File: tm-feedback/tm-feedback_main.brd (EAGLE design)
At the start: 60.1 x 40.3 mm, 45 parts

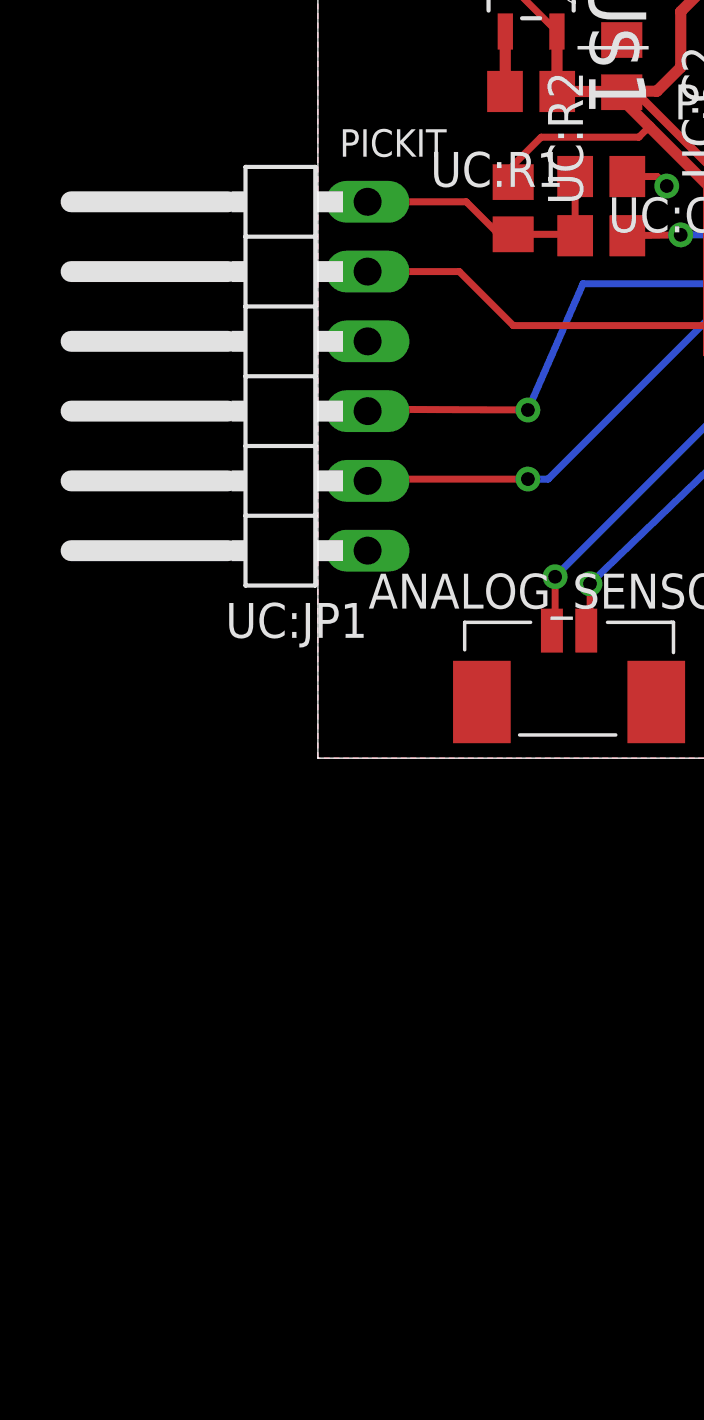
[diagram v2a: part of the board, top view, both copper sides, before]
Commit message: Replace PICKIT header with new header
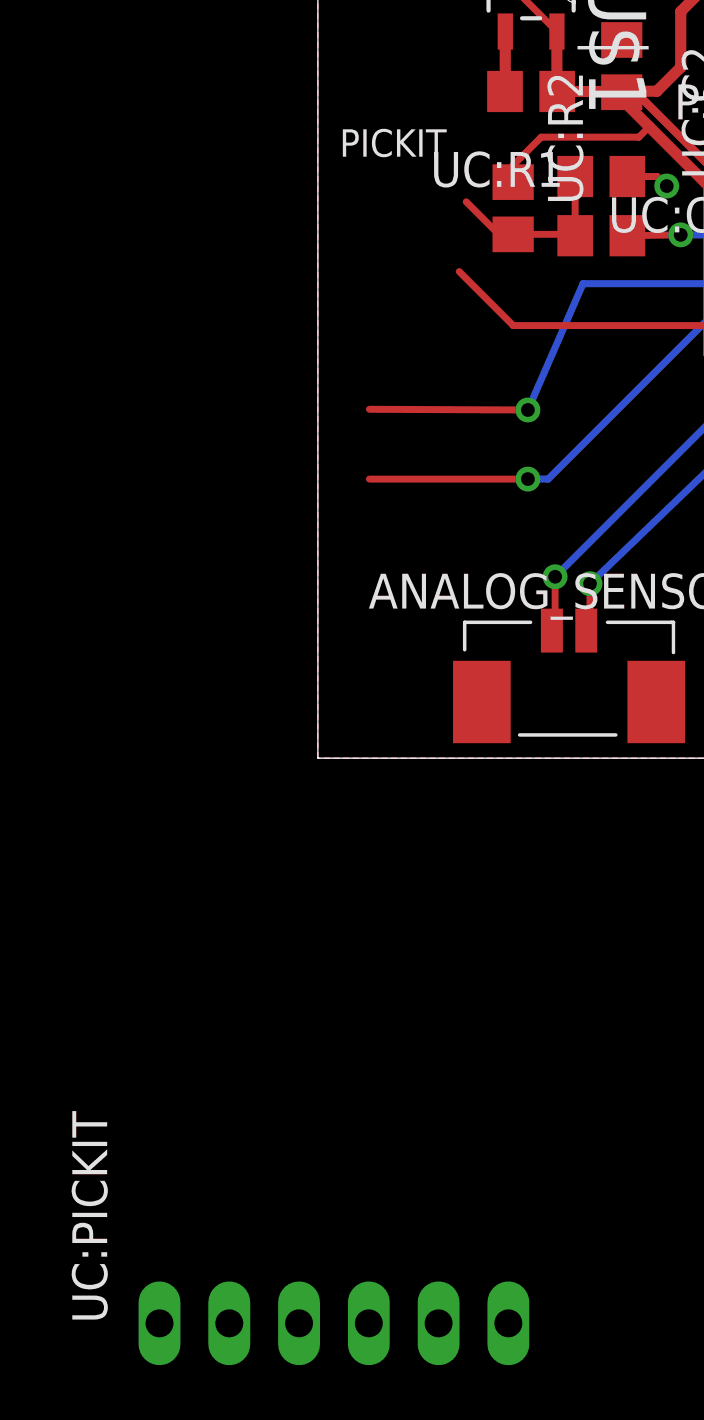
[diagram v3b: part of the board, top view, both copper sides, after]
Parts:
- removed UC:JP1: PICKIT, pinhead:1X06/90
- added UC:PICKIT: JP1, tactile-music:1X06/90
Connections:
- net +3V3: now also UC:PICKIT.5; no longer UC:JP1.5
- net GND: now also UC:PICKIT.4; no longer UC:JP1.4
- net UC:!MCLR: now also UC:PICKIT.6; no longer UC:JP1.6
- net UC:PGC: now also UC:PICKIT.2; no longer UC:JP1.2
- net UC:PGD: now also UC:PICKIT.3; no longer UC:JP1.3
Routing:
- net UC:!MCLR: track 10.2 -> 6.65 mm
- net +3V3: track 151.8 -> 148.5 mm
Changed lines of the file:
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@@
 <attribute name="VALUE" x="42.475" y="1.506" size="1.27" layer="27"/>
-</element>
-<element name="UC:JP1" library="pinhead" package="1X06/90" value="PICKIT" x="-2" y="13.904" smashed="yes" rot="R90">
-<attribute name="NAME" x="1.81" y="5.649" size="1.27" layer="25" ratio="10" rot="R180"/>
-<attribute name="VALUE" x="1.81" y="23.429" size="1.27" layer="27" rot="R180"/>
 </element>
 <element name="UC:JP2" library="pinhead" package="1X04/90" value="UART_PC" x="23.2664" y="-2.032" smashed="yes" rot="R180">
@@
 </element>
 <element name="BTN:PAIRING_SW" library="tactile-music" package="THRU-TACTILE-BTN" value="MC32881_TACTILE" x="38.6828" y="1.614" smashed="yes" rot="MR0"/>
+<element name="UC:PICKIT" library="tactile-music" package="1X06/90" value="JP1" x="0.5842" y="-16.764"/>
 </elements>
 <signals>
@@
 <contactref element="UC:C6" pad="2"/>
 <contactref element="UC:C7" pad="2"/>
-<contactref element="UC:JP1" pad="4"/>
 <contactref element="UC:LED2" pad="C"/>
 <contactref element="UC:LED1" pad="C"/>
@@
 <wire x1="17.018" y1="23.1902" x2="15.9058" y2="23.1902" width="0.4064" layer="1"/>
 <wire x1="15.9058" y1="23.1902" x2="15.8" y2="23.296" width="0.4064" layer="1"/>
+<contactref element="UC:PICKIT" pad="4"/>
+<wire x1="47.8562" y1="31.2774" x2="56.37" y2="24.5036" width="0" layer="19" extent="1-1"/>
+<wire x1="45.47" y1="24.5036" x2="47.8562" y2="31.2774" width="0" layer="19" extent="1-1"/>
+<wire x1="41.308" y1="24.712" x2="45.47" y2="24.5036" width="0" layer="19" extent="1-1"/>
+<wire x1="41.338" y1="18.722" x2="41.308" y2="24.712" width="0" layer="19" extent="1-1"/>
+<wire x1="42.238" y1="14.658" x2="42.926" y2="18.288" width="0" layer="19" extent="1-16"/>
+<wire x1="45.47" y1="13.0036" x2="42.926" y2="13.97" width="0" layer="19" extent="1-1"/>
+<wire x1="36.322" y1="19.304" x2="41.338" y2="18.722" width="0" layer="19" extent="1-1"/>
+<wire x1="30.318" y1="20.444" x2="34.524" y2="18.868" width="0" layer="19" extent="1-1"/>
+<wire x1="39.1448" y1="8.0856" x2="41.434" y2="14.658" width="0" layer="19" extent="1-1"/>
+<wire x1="40.06" y1="6.146" x2="39.1448" y2="8.0856" width="0" layer="19" extent="1-1"/>
+<wire x1="36.1828" y1="1.614" x2="40.06" y2="6.146" width="0" layer="19" extent="1-1"/>
+<wire x1="25.418" y1="14.744" x2="30.318" y2="20.444" width="0" layer="19" extent="1-1"/>
+<wire x1="20.744" y1="8.962" x2="25.2222" y2="12.6238" width="0" layer="19" extent="1-1"/>
+<wire x1="25.696" y1="6.508" x2="20.744" y2="8.962" width="0" layer="19" extent="1-1"/>
+<wire x1="27.882" y1="6.502" x2="25.696" y2="6.508" width="0" layer="19" extent="1-1"/>
+<wire x1="27.0764" y1="1.778" x2="27.882" y2="6.502" width="0" layer="19" extent="1-1"/>
+<wire x1="48.56" y1="2.072" x2="41.656" y2="5.334" width="0" layer="19" extent="1-16"/>
+<wire x1="33.49" y1="27.73" x2="30.318" y2="20.444" width="0" layer="19" extent="1-1"/>
+<wire x1="24.618" y1="26.144" x2="30.318" y2="20.444" width="0" layer="19" extent="1-1"/>
+<wire x1="23.8576" y1="30.7236" x2="24.618" y2="26.144" width="0" layer="19" extent="1-1"/>
+<wire x1="26.911" y1="35.548" x2="23.8576" y2="30.7236" width="0" layer="19" extent="1-1"/>
+<wire x1="18.918" y1="21.244" x2="24.618" y2="26.144" width="0" layer="19" extent="1-1"/>
+<wire x1="15.7988" y1="24.892" x2="15.8" y2="23.824" width="0" layer="19" extent="1-1"/>
+<wire x1="15.652" y1="26.32" x2="15.7988" y2="24.892" width="0" layer="19" extent="1-1"/>
+<wire x1="12.7" y1="20.828" x2="15.8" y2="23.296" width="0" layer="19" extent="1-1"/>
+<wire x1="11.062" y1="26.144" x2="15.652" y2="26.444" width="0" layer="19" extent="1-1"/>
+<wire x1="7.762" y1="29.1956" x2="11.062" y2="26.144" width="0" layer="19" extent="1-1"/>
+<wire x1="9.918" y1="32.946" x2="7.762" y2="29.1956" width="0" layer="19" extent="1-1"/>
+<wire x1="9.5212" y1="36.8528" x2="9.918" y2="32.946" width="0" layer="19" extent="1-1"/>
+<wire x1="14.668" y1="31.136" x2="15.652" y2="26.444" width="0" layer="19" extent="1-1"/>
+<wire x1="56.37" y1="13.0036" x2="45.47" y2="13.0036" width="0" layer="19" extent="1-1"/>
+<wire x1="56.8884" y1="9.645" x2="56.37" y2="13.0036" width="0" layer="19" extent="1-1"/>
+<wire x1="1.8542" y1="-20.574" x2="27.0764" y2="1.778" width="0" layer="19" extent="1-1"/>
 </signal>
 <signal name="BT:N$6">
@@
 <contactref element="UC:R1" pad="1"/>
 <contactref element="UC:R2" pad="1"/>
-<contactref element="UC:JP1" pad="6"/>
 <contactref element="UC:C1" pad="1"/>
-<wire x1="1.81" y1="20.254" x2="5.4" y2="20.254" width="0.254" layer="1"/>
 <wire x1="5.4" y1="20.254" x2="6.604" y2="19.05" width="0.254" layer="1"/>
 <wire x1="6.604" y1="19.05" x2="7.088" y2="19.05" width="0.254" layer="1"/>
@@
 <wire x1="9.316" y1="19.07" x2="9.366" y2="19.02" width="0.254" layer="1"/>
 <wire x1="9.366" y1="19.02" x2="9.366" y2="21.174" width="0.254" layer="1"/>
+<contactref element="UC:PICKIT" pad="6"/>
+<wire x1="6.9342" y1="-20.574" x2="6.604" y2="19.05" width="0" layer="19" extent="1-1"/>
 </signal>
 <signal name="UC:PGD">
-<contactref element="UC:JP1" pad="3"/>
 <contactref element="UC:U1" pad="21"/>
 <wire x1="18.918" y1="17.244" x2="16.792" y2="17.244" width="0.254" layer="1"/>
@@
 <via x="7.6454" y="12.6746" extent="1-16" drill="0.5"/>
 <wire x1="7.6454" y1="12.6746" x2="1.876" y2="12.7" width="0.254" layer="1"/>
-<wire x1="1.876" y1="12.7" x2="1.81" y2="12.634" width="0.254" layer="1"/>
+<contactref element="UC:PICKIT" pad="3"/>
+<wire x1="1.876" y1="12.7" x2="-0.6858" y2="-20.574" width="0" layer="19" extent="1-1"/>
 </signal>
 <signal name="UC:PGC">
-<contactref element="UC:JP1" pad="2"/>
 <contactref element="UC:U1" pad="22"/>
 <wire x1="18.918" y1="16.444" x2="17.46" y2="16.444" width="0.254" layer="1"/>
@@
 <via x="7.6454" y="10.16" extent="1-16" drill="0.5"/>
 <wire x1="7.6454" y1="10.16" x2="1.876" y2="10.16" width="0.254" layer="1"/>
-<wire x1="1.876" y1="10.16" x2="1.81" y2="10.094" width="0.254" layer="1"/>
 <wire x1="7.6454" y1="10.16" x2="8.382" y2="10.16" width="0.254" layer="16"/>
 <wire x1="8.382" y1="10.16" x2="14.224" y2="16.002" width="0.254" layer="16"/>
 <wire x1="14.224" y1="16.002" x2="17.018" y2="16.002" width="0.254" layer="16"/>
+<contactref element="UC:PICKIT" pad="2"/>
+<wire x1="1.876" y1="10.16" x2="-3.2258" y2="-20.574" width="0" layer="19" extent="1-1"/>
 </signal>
 <signal name="UC:N$3">
@@
 <contactref element="UC:C5" pad="1"/>
 <contactref element="UC:U1" pad="40"/>
-<contactref element="UC:JP1" pad="5"/>
 <contactref element="BTN:R1" pad="2"/>
 <contactref element="BTN:U1" pad="5"/>
@@
 <wire x1="18.034" y1="10.922" x2="20.684" y2="10.922" width="0.4064" layer="1"/>
 <wire x1="20.684" y1="10.922" x2="20.744" y2="10.862" width="0.254" layer="1"/>
-<wire x1="1.81" y1="17.714" x2="5.146" y2="17.714" width="0.254" layer="1"/>
 <wire x1="5.146" y1="17.714" x2="7.112" y2="15.748" width="0.254" layer="1"/>
 <wire x1="7.112" y1="15.748" x2="14.224" y2="15.748" width="0.254" layer="1"/>
@@
 <wire x1="12.3422" y1="24.2802" x2="11.0982" y2="24.2802" width="0.4064" layer="1"/>
 <wire x1="11.0982" y1="24.2802" x2="11.062" y2="24.244" width="0.254" layer="1"/>
+<contactref element="UC:PICKIT" pad="5"/>
+<wire x1="4.3942" y1="-20.574" x2="18.034" y2="10.922" width="0" layer="19" extent="1-1"/>
 </signal>
 <signal name="BTN:N$2">
